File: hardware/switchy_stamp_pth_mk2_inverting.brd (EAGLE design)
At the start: 38.1 x 25.4 mm, 23 parts, among them IC1 MC34063

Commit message: fixed a few mistakes, still rearranging
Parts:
- removed U$1: (no value), A_butts:CC-BY-SA-4.0-NO-URL
- removed U$2: (no value), A_butts:COW_SMALL
- removed U$3: (no value), A_butts:OSHWLOGO_BOT_0.2_A
- C1: value 68uF -> 100uF
- H1, H2, H3, H4: value HOLE#4 -> HOLE#2; device A_butts:HOLE-#4 -> A_butts:HOLE-#2
- L1: device A_butts:RLB0912 -> A_butts:RADIAL-PTH-3-BY-6.7DIA
- ON/OFF: value SWITCH-SPDTPTH-RA-2.54MM -> SWITCH-SPDTPTH-VERT-2.54MM; device A_butts:SPDT-RA-2.54MM -> A_butts:SWITCH-SPDT
- R3: device A_butts:RESISTOR-AXIAL-PTH-10.16MM -> A_butts:RESISTOR-AXIAL-PTH-7.68MM
- moved H4 51.3 mm to (46.6, 32.1)
- moved D2 27.5 mm to (33.0, 27.9), turned to 270 degrees
- moved H1 25.2 mm to (11.0, 11.8)
- moved F1 21.1 mm to (11.9, 28.6), turned to 0 degrees
- moved IN 18.6 mm to (17.0, 28.6), turned to 0 degrees
- moved ON/OFF 17.4 mm to (18.9, 17.8)
- moved IC1 16.0 mm to (26.5, 24.1)
- moved R2 15.8 mm to (26.7, 33.0), turned to 0 degrees
- moved H3 15.8 mm to (43.2, 16.9)
- moved R1 15.5 mm to (26.7, 30.6), turned to 180 degrees
- moved C3 15.2 mm to (35.7, 24.1), turned to 270 degrees
- moved D1 15.2 mm to (15.2, 25.4), turned to 0 degrees
- moved R3 15.1 mm to (26.5, 17.7), turned to 0 degrees
- moved OUT 13.3 mm to (42.3, 23.9), turned to 0 degrees
- moved H2 12.8 mm to (11.0, 32.1)
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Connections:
- net GND: now also L1.P$2; no longer L1.2
- net N$6: now also L1.P$1
- net VOUT-: no longer L1.1
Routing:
- net VOUT-: track 31.9 -> 0.00 mm
- net N$5: track 14.3 -> 0.00 mm
- net N$7: track 14.2 -> 0.00 mm
- net N$1: track 12.7 -> 0.00 mm
- net N$6: track 8.39 -> 0.00 mm
- net N$8: track 7.56 -> 0.00 mm
- net VIN+: track 6.10 -> 0.00 mm
- net N$3: track 5.33 -> 0.00 mm
- net N$4: track 4.29 -> 0.00 mm
- net N$2: track 2.79 -> 0.00 mm
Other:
- board size 38.1 x 25.4 mm -> 40.6 x 36.2 mm

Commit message: redo
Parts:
- R1, R2: device A_butts:RESISTOR-AXIAL-PTH-5.08MM -> A_butts:RESISTOR-AXIAL-PTH-7.68MM
- moved H4 31.6 mm to (35.6, 2.54)
- moved D2 26.9 mm to (23.5, 2.79), turned to 180 degrees
- moved F1 21.4 mm to (3.81, 8.76), turned to 180 degrees
- moved IN 20.1 mm to (6.10, 11.7), turned to 90 degrees
- moved ON/OFF 17.3 mm to (10.7, 2.54), turned to 90 degrees
- moved C2 16.1 mm to (28.1, 21.5), turned to 0 degrees
- moved R2 16.1 mm to (18.9, 18.9)
- moved D1 15.0 mm to (9.91, 11.4), turned to 90 degrees
- moved R3 14.7 mm to (12.7, 12.6), turned to 270 degrees
- moved OUT 14.6 mm to (32.0, 13.5), turned to 270 degrees
- moved IC1 13.8 mm to (18.9, 12.6)
- moved C3 13.8 mm to (25.3, 15.1), turned to 90 degrees
- moved LED1 12.8 mm to (35.1, 6.99), turned to 180 degrees
- moved H1 12.6 mm to (2.54, 2.54)
- moved H2 12.6 mm to (2.54, 22.9)
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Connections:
- net N$4: now also F1.P$1; no longer ON/OFF.2
- net N$8: now also F1.P$2, ON/OFF.2; no longer F1.P$1, ON/OFF.1
- net VIN+: now also ON/OFF.3; no longer F1.P$2
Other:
- board size 40.6 x 36.2 mm -> 38.1 x 25.4 mm

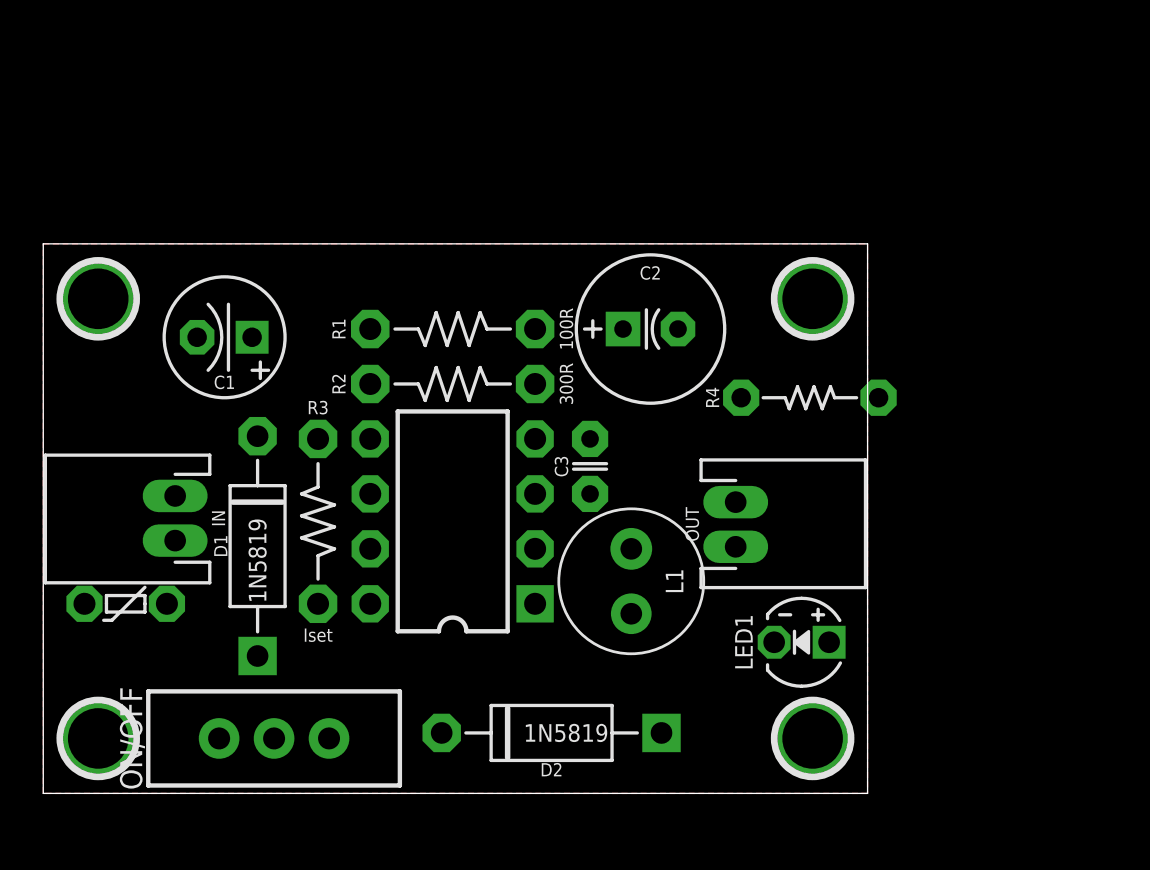
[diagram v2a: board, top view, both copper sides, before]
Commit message: a saner layout with a few fixes, but still not complete
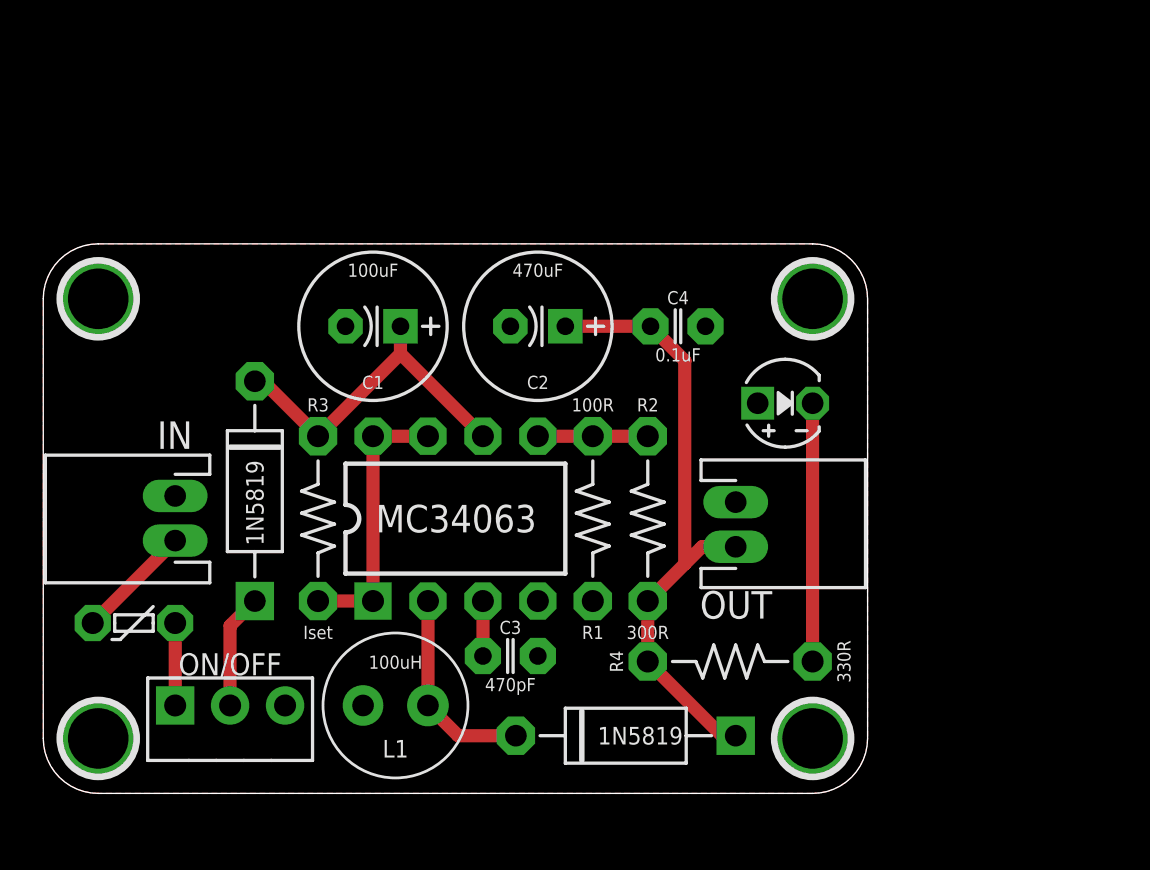
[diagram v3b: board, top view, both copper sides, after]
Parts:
- added C4: 0.1uF, A_butts:C025-024X044
- C1: device A_butts:E2,5-6 -> A_butts:E2,5-7
- IN, OUT: device A_butts:JST-2-PTH -> A_butts:JST-2-PH-RA-PTH
- ON/OFF: value SWITCH-SPDTPTH-VERT-2.54MM -> SWITCH-SPDTPTH-RA-2.54MM; device A_butts:SWITCH-SPDT -> A_butts:SPDT-RA-2.54MM
- R4: device A_butts:RESISTOR-AXIAL-PTH-5.08MM -> A_butts:RESISTOR-AXIAL-PTH-7.68MM
- moved R4 12.7 mm to (31.8, 6.10)
- moved L1 11.9 mm to (17.8, 4.06), turned to 180 degrees
- moved LED1 11.1 mm to (34.3, 18.0), turned to 0 degrees
- moved R2 11.0 mm to (27.9, 12.7), turned to 270 degrees
- moved R1 10.9 mm to (25.4, 12.7), turned to 90 degrees
- moved C3 9.51 mm to (21.6, 6.35), turned to 0 degrees
- moved C1 6.88 mm to (15.2, 21.6)
- moved C2 5.21 mm to (22.9, 21.6), turned to 180 degrees
- moved ON/OFF 4.82 mm to (6.10, 4.06), turned to 0 degrees
- moved D2 3.43 mm to (26.9, 2.67)
- moved D1 2.54 mm to (9.78, 14.0)
- moved F1 0.97 mm to (4.19, 7.87)
- moved IC1 0.18 mm to (19.1, 12.7), turned to 0 degrees
- moved R3 0.13 mm to (12.7, 12.7)
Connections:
- net GND: now also C4.2
- net N$4: now also ON/OFF.1; no longer D1.A
- net N$8: now also D1.A; no longer F1.P$2
- net VIN+: now also F1.P$2; no longer ON/OFF.3
- net VOUT-: now also C4.1
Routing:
- net VOUT-: track 0.00 -> 29.0 mm
- net N$5: track 0.00 -> 16.0 mm
- net N$1: track 0.00 -> 12.7 mm
- net N$7: track 0.00 -> 11.9 mm
- net N$6: track 0.00 -> 9.47 mm
- net VIN+: track 0.00 -> 5.39 mm
- net N$8: track 0.00 -> 5.30 mm
- net N$3: track 0.00 -> 5.08 mm
- net N$4: track 0.00 -> 3.81 mm
- net N$2: track 0.00 -> 2.54 mm
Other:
- outline, holes or cut-outs redrawn

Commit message: blah
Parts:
- added U$1, U$2: (no value), A_butts:CC-BY-SA-4.0-NO-URL
- added U$3: (no value), A_butts:COW
- added U$4: (no value), A_butts:COW_SMALL
- added U$5: (no value), A_butts:OSHWLOGO_BOT_0.2_A
- added U$6: (no value), A_butts:OSHWLOGO_TOP_0.2_A
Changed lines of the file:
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@@
 <?xml version="1.0" encoding="utf-8"?>
 <!DOCTYPE eagle SYSTEM "eagle.dtd">
-<eagle version="6.5.0">
+<eagle version="6.4">
 <drawing>
 <settings>
@@
 <element name="OUT" library="A_butts" package="JST-2-PH-RA-PTH" value="M02JST-PTH-2" x="32.004" y="13.462" smashed="yes" rot="R270">
 <attribute name="SKU" value="PRT-09914" x="29.464" y="-23.368" size="1.778" layer="27" rot="R270" display="off"/>
-<attribute name="NAME" x="32.02" y="9.349" size="1.27" layer="25" font="vector" ratio="12" rot="R180" align="bottom-center"/>
+<attribute name="NAME" x="36.084" y="9.222" size="1.27" layer="25" font="vector" ratio="12" rot="R180" align="bottom-center"/>
 </element>
 <element name="IN" library="A_butts" package="JST-2-PH-RA-PTH" value="M02JST-PTH-2" x="6.096" y="11.684" smashed="yes" rot="R90">
 <attribute name="SKU" value="PRT-09914" x="8.636" y="42.164" size="1.778" layer="27" rot="R90" display="off"/>
-<attribute name="NAME" x="6.08" y="15.924" size="1.27" layer="25" font="vector" ratio="12" align="bottom-center"/>
+<attribute name="NAME" x="1.508" y="16.051" size="1.27" layer="25" font="vector" ratio="12" align="bottom-center"/>
 </element>
 <element name="IC1" library="A_butts" package="DIP-08" value="MC34063" x="19.05" y="12.7" smashed="yes">
@@
 <attribute name="VALUE" x="29.337" y="20.574" size="0.6096" layer="21" font="vector" ratio="12" rot="R180" align="bottom-center"/>
 </element>
+<element name="U$1" library="A_butts" package="CC-BY-SA-4.0-NO-URL" value="" x="6.604" y="23.241"/>
+<element name="U$2" library="A_butts" package="CC-BY-SA-4.0-NO-URL" value="" x="2.667" y="10.414" rot="MR90"/>
+<element name="U$3" library="A_butts" package="COW" value="" x="40.767" y="19.304" rot="MR270"/>
+<element name="U$4" library="A_butts" package="COW_SMALL" value="" x="19.812" y="12.7" rot="MR90"/>
+<element name="U$5" library="A_butts" package="OSHWLOGO_BOT_0.2_A" value="" x="2.794" y="17.907" rot="R270"/>
+<element name="U$6" library="A_butts" package="OSHWLOGO_TOP_0.2_A" value="" x="5.334" y="18.161"/>
 </elements>
 <signals>
@@
 <contactref element="R3" pad="P$2"/>
 <contactref element="IC1" pad="7"/>
-<wire x1="15.24" y1="16.51" x2="17.78" y2="16.51" width="0.6096" layer="1"/>
-<wire x1="15.24" y1="8.89" x2="12.7" y2="8.89" width="0.6096" layer="1"/>
-<wire x1="15.24" y1="8.89" x2="15.24" y2="16.51" width="0.6096" layer="1"/>
+<wire x1="15.24" y1="16.51" x2="17.78" y2="16.51" width="0.4064" layer="1"/>
+<wire x1="15.24" y1="8.89" x2="12.7" y2="8.89" width="0.4064" layer="1"/>
+<wire x1="15.24" y1="8.89" x2="15.24" y2="16.51" width="0.4064" layer="1"/>
 </signal>
 <signal name="N$2">
@@
 <contactref element="R2" pad="P$1"/>
 <contactref element="IC1" pad="5"/>
-<wire x1="22.86" y1="16.51" x2="25.4" y2="16.51" width="0.6096" layer="1"/>
-<wire x1="25.4" y1="16.51" x2="27.94" y2="16.51" width="0.6096" layer="1"/>
+<wire x1="22.86" y1="16.51" x2="25.4" y2="16.51" width="0.4064" layer="1"/>
+<wire x1="25.4" y1="16.51" x2="27.94" y2="16.51" width="0.4064" layer="1"/>
 </signal>
 <signal name="GND">
@@
 <contactref element="D2" pad="A"/>
 <contactref element="C4" pad="1"/>
-<wire x1="24.13" y1="21.59" x2="28.067" y2="21.59" width="0.6096" layer="1"/>
+<wire x1="24.13" y1="21.59" x2="28.067" y2="21.59" width="0.4064" layer="1"/>
 <wire x1="27.94" y1="8.89" x2="29.6545" y2="10.6045" width="0.6096" layer="1"/>
 <wire x1="29.6545" y1="10.6045" x2="30.448" y2="11.398" width="0.6096" layer="1"/>
 <wire x1="30.448" y1="11.398" x2="32.004" y2="11.398" width="0.6096" layer="1"/>
-<wire x1="28.067" y1="21.59" x2="29.6545" y2="20.0025" width="0.6096" layer="1"/>
-<wire x1="29.6545" y1="20.0025" x2="29.6545" y2="10.6045" width="0.6096" layer="1"/>
+<wire x1="28.067" y1="21.59" x2="29.6545" y2="20.0025" width="0.4064" layer="1"/>
+<wire x1="29.6545" y1="20.0025" x2="29.6545" y2="10.6045" width="0.4064" layer="1"/>
 <wire x1="27.94" y1="8.89" x2="27.94" y2="6.096" width="0.6096" layer="1"/>
 <wire x1="27.94" y1="6.096" x2="31.369" y2="2.667" width="0.6096" layer="1"/>
@@
 <contactref element="LED1" pad="K"/>
 <contactref element="R4" pad="P$2"/>
-<wire x1="35.56" y1="6.096" x2="35.56" y2="18.034" width="0.6096" layer="1"/>
+<wire x1="35.56" y1="6.096" x2="35.56" y2="18.034" width="0.4064" layer="1"/>
 </signal>
 <signal name="N$6">
